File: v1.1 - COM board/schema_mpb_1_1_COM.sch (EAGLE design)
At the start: 27 parts, among them IC1 E73_2G4M04S, IC3 PCA82C250, U1 ESP-WROOM-32

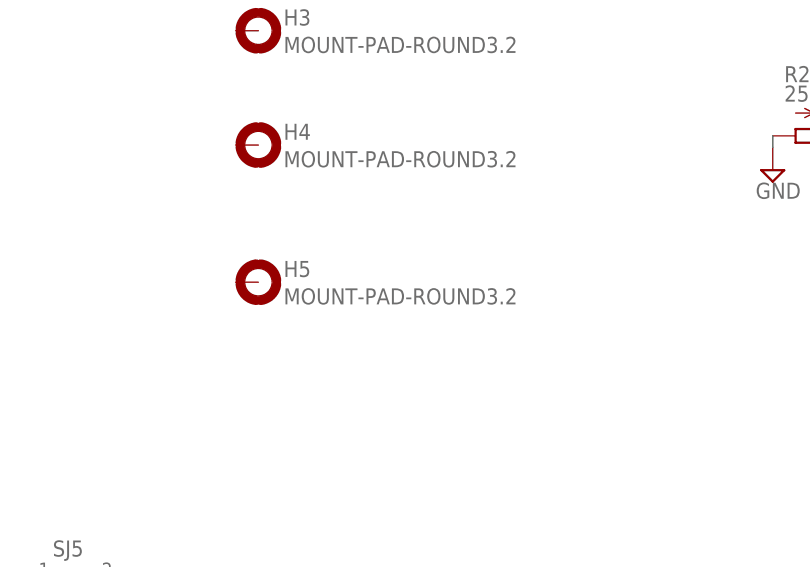
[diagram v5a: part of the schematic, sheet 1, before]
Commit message: COM revision
- Added Ethernet module outline
- Adjusted track width
- labelled CAN terminals
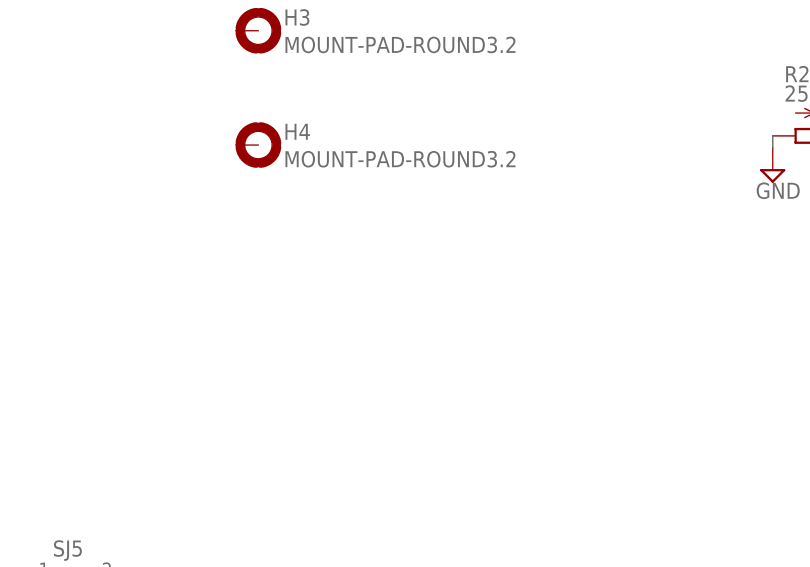
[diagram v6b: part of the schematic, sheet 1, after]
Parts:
- removed H5: MOUNT-PAD-ROUND3.2, holes:MOUNT-PAD-ROUND3.2
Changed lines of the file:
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@@
 <grid distance="0.1" unitdist="inch" unit="mm" style="dots" multiple="1" display="yes" altdistance="0.01" altunitdist="inch" altunit="inch"/>
 <layers>
-<layer number="1" name="Top" color="4" fill="1" visible="yes" active="no"/>
-<layer number="2" name="Route2" color="1" fill="3" visible="yes" active="no"/>
-<layer number="3" name="Route3" color="4" fill="3" visible="yes" active="no"/>
-<layer number="4" name="Route4" color="1" fill="4" visible="yes" active="no"/>
-<layer number="5" name="Route5" color="4" fill="4" visible="yes" active="no"/>
-<layer number="6" name="Route6" color="1" fill="8" visible="yes" active="no"/>
-<layer number="7" name="Route7" color="4" fill="8" visible="yes" active="no"/>
-<layer number="8" name="Route8" color="1" fill="2" visible="yes" active="no"/>
-<layer number="9" name="Route9" color="4" fill="2" visible="yes" active="no"/>
-<layer number="10" name="Route10" color="1" fill="7" visible="yes" active="no"/>
-<layer number="11" name="Route11" color="4" fill="7" visible="yes" active="no"/>
-<layer number="12" name="Route12" color="1" fill="5" visible="yes" active="no"/>
-<layer number="13" name="Route13" color="4" fill="5" visible="yes" active="no"/>
-<layer number="14" name="Route14" color="1" fill="6" visible="yes" active="no"/>
-<layer number="15" name="Route15" color="4" fill="6" visible="yes" active="no"/>
-<layer number="16" name="Bottom" color="1" fill="1" visible="yes" active="no"/>
-<layer number="17" name="Pads" color="2" fill="1" visible="yes" active="no"/>
-<layer number="18" name="Vias" color="2" fill="1" visible="yes" active="no"/>
-<layer number="19" name="Unrouted" color="6" fill="1" visible="yes" active="no"/>
-<layer number="20" name="Dimension" color="24" fill="1" visible="yes" active="no"/>
-<layer number="21" name="tPlace" color="7" fill="1" visible="yes" active="no"/>
-<layer number="22" name="bPlace" color="7" fill="1" visible="yes" active="no"/>
-<layer number="23" name="tOrigins" color="15" fill="1" visible="yes" active="no"/>
-<layer number="24" name="bOrigins" color="15" fill="1" visible="yes" active="no"/>
-<layer number="25" name="tNames" color="7" fill="1" visible="yes" active="no"/>
-<layer number="26" name="bNames" color="7" fill="1" visible="yes" active="no"/>
-<layer number="27" name="tValues" color="7" fill="1" visible="yes" active="no"/>
-<layer number="28" name="bValues" color="7" fill="1" visible="yes" active="no"/>
+<layer number="1" name="Top" color="4" fill="1" visible="no" active="no"/>
+<layer number="2" name="Route2" color="1" fill="3" visible="no" active="no"/>
+<layer number="3" name="Route3" color="4" fill="3" visible="no" active="no"/>
+<layer number="4" name="Route4" color="1" fill="4" visible="no" active="no"/>
+<layer number="5" name="Route5" color="4" fill="4" visible="no" active="no"/>
+<layer number="6" name="Route6" color="1" fill="8" visible="no" active="no"/>
+<layer number="7" name="Route7" color="4" fill="8" visible="no" active="no"/>
+<layer number="8" name="Route8" color="1" fill="2" visible="no" active="no"/>
+<layer number="9" name="Route9" color="4" fill="2" visible="no" active="no"/>
+<layer number="10" name="Route10" color="1" fill="7" visible="no" active="no"/>
+<layer number="11" name="Route11" color="4" fill="7" visible="no" active="no"/>
+<layer number="12" name="Route12" color="1" fill="5" visible="no" active="no"/>
+<layer number="13" name="Route13" color="4" fill="5" visible="no" active="no"/>
+<layer number="14" name="Route14" color="1" fill="6" visible="no" active="no"/>
+<layer number="15" name="Route15" color="4" fill="6" visible="no" active="no"/>
+<layer number="16" name="Bottom" color="1" fill="1" visible="no" active="no"/>
+<layer number="17" name="Pads" color="2" fill="1" visible="no" active="no"/>
+<layer number="18" name="Vias" color="2" fill="1" visible="no" active="no"/>
+<layer number="19" name="Unrouted" color="6" fill="1" visible="no" active="no"/>
+<layer number="20" name="Dimension" color="24" fill="1" visible="no" active="no"/>
+<layer number="21" name="tPlace" color="7" fill="1" visible="no" active="no"/>
+<layer number="22" name="bPlace" color="7" fill="1" visible="no" active="no"/>
+<layer number="23" name="tOrigins" color="15" fill="1" visible="no" active="no"/>
+<layer number="24" name="bOrigins" color="15" fill="1" visible="no" active="no"/>
+<layer number="25" name="tNames" color="7" fill="1" visible="no" active="no"/>
+<layer number="26" name="bNames" color="7" fill="1" visible="no" active="no"/>
+<layer number="27" name="tValues" color="7" fill="1" visible="no" active="no"/>
+<layer number="28" name="bValues" color="7" fill="1" visible="no" active="no"/>
 <layer number="29" name="tStop" color="7" fill="3" visible="no" active="no"/>
 <layer number="30" name="bStop" color="7" fill="6" visible="no" active="no"/>
@@
 <layer number="35" name="tGlue" color="7" fill="4" visible="no" active="no"/>
 <layer number="36" name="bGlue" color="7" fill="5" visible="no" active="no"/>
-<layer number="37" name="tTest" color="7" fill="1" visible="yes" active="no"/>
-<layer number="38" name="bTest" color="7" fill="1" visible="yes" active="no"/>
+<layer number="37" name="tTest" color="7" fill="1" visible="no" active="no"/>
+<layer number="38" name="bTest" color="7" fill="1" visible="no" active="no"/>
 <layer number="39" name="tKeepout" color="4" fill="11" visible="no" active="no"/>
 <layer number="40" name="bKeepout" color="1" fill="11" visible="no" active="no"/>
@@
 <layer number="44" name="Drills" color="7" fill="1" visible="no" active="no"/>
 <layer number="45" name="Holes" color="7" fill="1" visible="no" active="no"/>
-<layer number="46" name="Milling" color="3" fill="1" visible="yes" active="no"/>
-<layer number="47" name="Measures" color="7" fill="1" visible="yes" active="no"/>
-<layer number="48" name="Document" color="7" fill="1" visible="yes" active="no"/>
-<layer number="49" name="Reference" color="7" fill="1" visible="yes" active="no"/>
-<layer number="50" name="dxf" color="7" fill="1" visible="yes" active="no"/>
-<layer number="51" name="tDocu" color="7" fill="1" visible="yes" active="no"/>
-<layer number="52" name="bDocu" color="7" fill="1" visible="yes" active="no"/>
-<layer number="53" name="tGND_GNDA" color="7" fill="9" visible="yes" active="no"/>
-<layer number="54" name="bGND_GNDA" color="1" fill="9" visible="yes" active="no"/>
-<layer number="56" name="wert" color="7" fill="1" visible="yes" active="no"/>
-<layer number="57" name="tCAD" color="7" fill="1" visible="yes" active="no"/>
+<layer number="46" name="Milling" color="3" fill="1" visible="no" active="no"/>
+<layer number="47" name="Measures" color="7" fill="1" visible="no" active="no"/>
+<layer number="48" name="Document" color="7" fill="1" visible="no" active="no"/>
+<layer number="49" name="Reference" color="7" fill="1" visible="no" active="no"/>
+<layer number="50" name="dxf" color="7" fill="1" visible="no" active="no"/>
+<layer number="51" name="tDocu" color="7" fill="1" visible="no" active="no"/>
+<layer number="52" name="bDocu" color="7" fill="1" visible="no" active="no"/>
+<layer number="53" name="tGND_GNDA" color="7" fill="9" visible="no" active="no"/>
+<layer number="54" name="bGND_GNDA" color="1" fill="9" visible="no" active="no"/>
+<layer number="56" name="wert" color="7" fill="1" visible="no" active="no"/>
+<layer number="57" name="tCAD" color="7" fill="1" visible="no" active="no"/>
 <layer number="59" name="tCarbon" color="7" fill="1" visible="no" active="no"/>
 <layer number="60" name="bCarbon" color="7" fill="1" visible="no" active="no"/>
@@
 <part name="H3" library="holes" library_urn="urn:adsk.eagle:library:237" deviceset="MOUNT-PAD-ROUND" device="3.2" package3d_urn="urn:adsk.eagle:package:14282/1"/>
 <part name="H4" library="holes" library_urn="urn:adsk.eagle:library:237" deviceset="MOUNT-PAD-ROUND" device="3.2" package3d_urn="urn:adsk.eagle:package:14282/1"/>
-<part name="H5" library="holes" library_urn="urn:adsk.eagle:library:237" deviceset="MOUNT-PAD-ROUND" device="3.2" package3d_urn="urn:adsk.eagle:package:14282/1"/>
 </parts>
 <sheets>
@@
 <instance part="H3" gate="G$1" x="182.88" y="152.4"/>
 <instance part="H4" gate="G$1" x="182.88" y="139.7"/>
-<instance part="H5" gate="G$1" x="182.88" y="124.46"/>
 </instances>
 <busses>
